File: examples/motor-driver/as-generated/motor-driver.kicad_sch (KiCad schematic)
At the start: 18 parts, among them J1 VM 2.7-10.8V, J2 MOTOR A, J3 MOTOR B, J4 LOGIC, U1 DRV8833PW

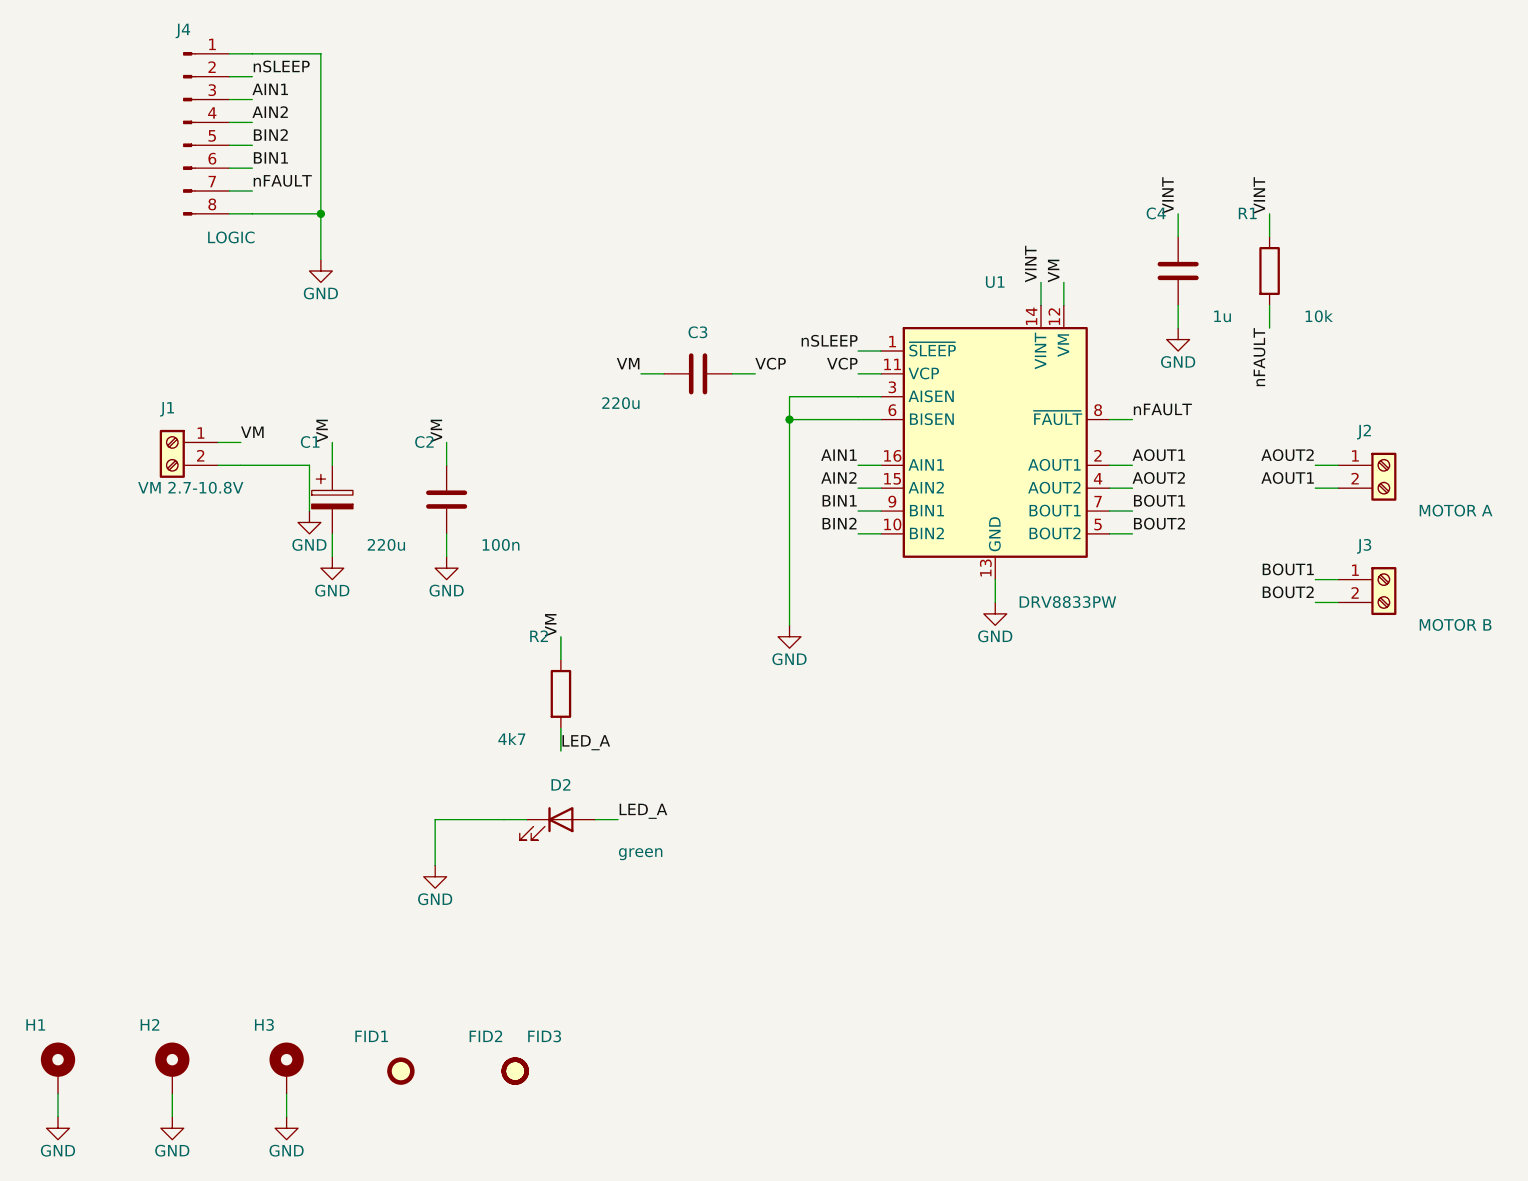
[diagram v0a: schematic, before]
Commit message: chore(examples): publish DRC-clean motor rebuild and verified copper renders
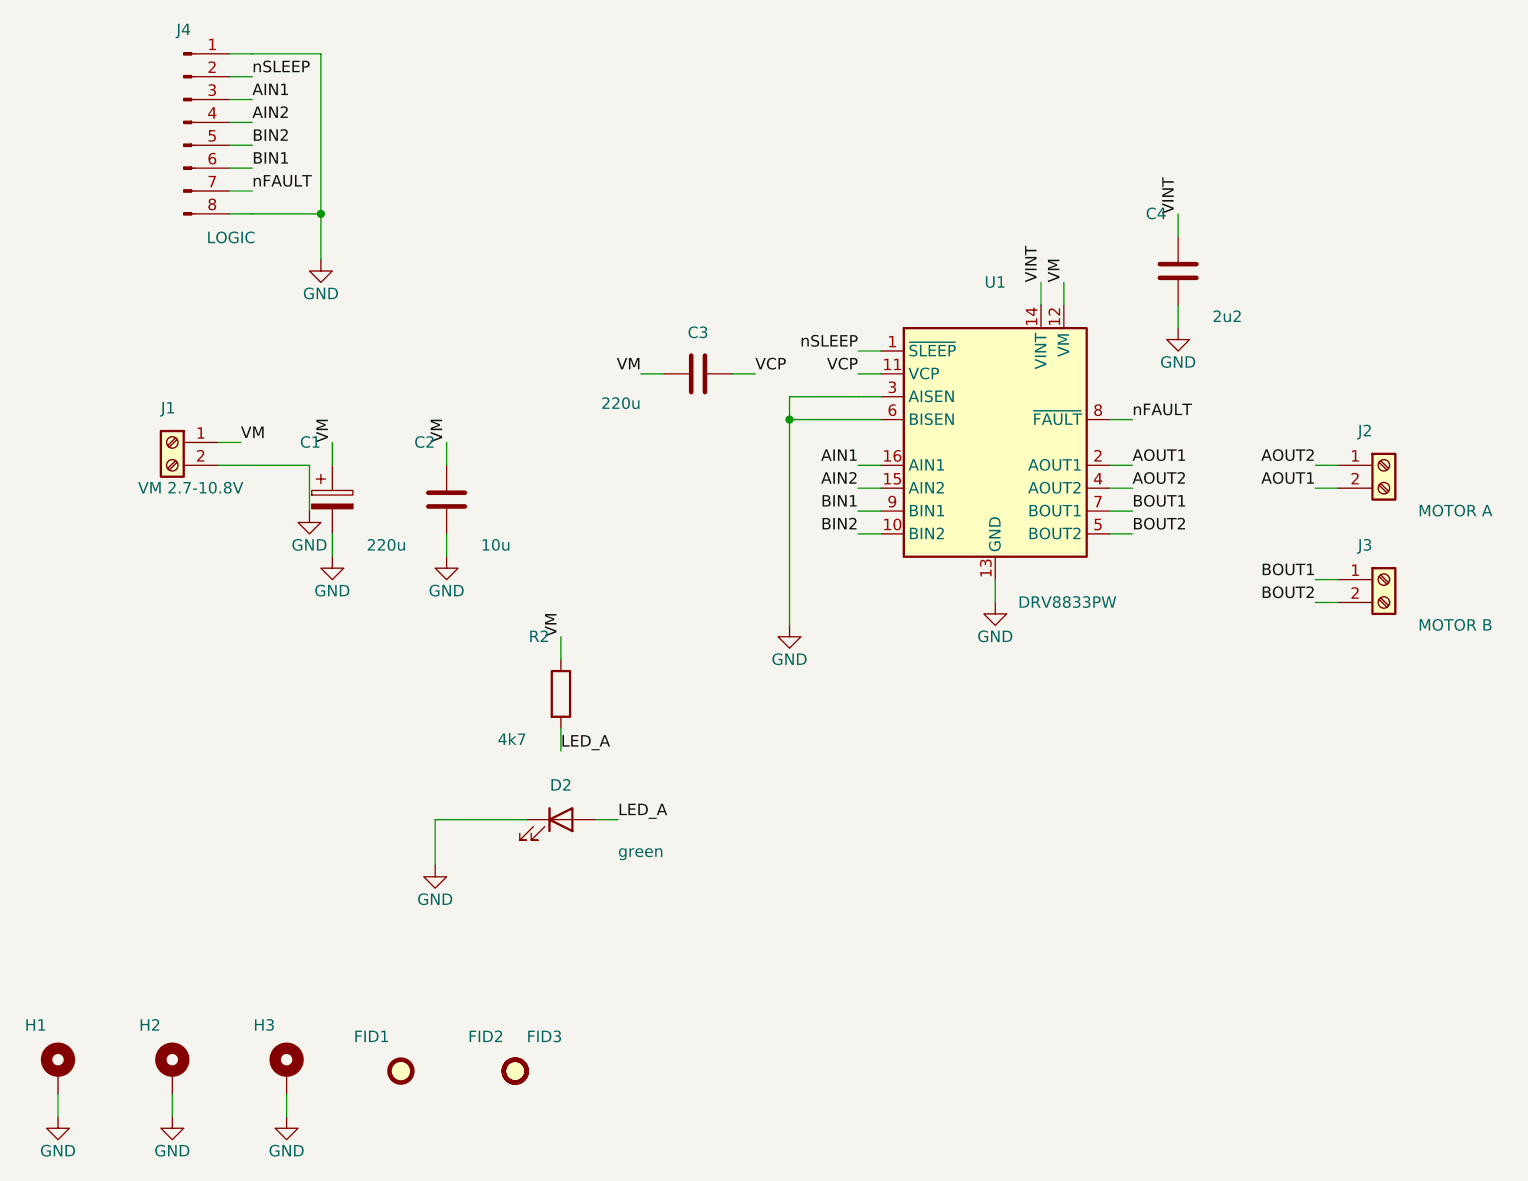
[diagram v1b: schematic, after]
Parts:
- removed R1: 10k, Resistor_SMD:R_0805_2012Metric, symbol Device:R
- C2: value 100n -> 10u
- C4: value 1u -> 2u2
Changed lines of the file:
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@@
     (exclude_from_sim no) (in_bom yes) (on_board yes) (dnp no)
     (property "Reference" "C2" (at 67.62 79.82 0) (effects (font (size 1.27 1.27)) (justify right)))
-    (property "Value" "100n" (at 72.7 91.25 0) (effects (font (size 1.27 1.27)) (justify left)))
+    (property "Value" "10u" (at 72.7 91.25 0) (effects (font (size 1.27 1.27)) (justify left)))
     (property "Footprint" "Capacitor_SMD:C_0805_2012Metric" (at 68.89 86.17 0) (effects (font (size 1.27 1.27)) hide))
-    (property "Datasheet" "https://product.samsungsem.com/mlcc/CL21B104KBCNNNC.do" (at 68.89 86.17 0) (effects (font (size 1.27 1.27)) hide))
+    (property "Datasheet" "https://weblib.samsungsem.com/mlcc/mlcc-ec-data-sheet.do?partNumber=CL21A106KAYNNN" (at 68.89 86.17 0) (effects (font (size 1.27 1.27)) hide))
     (pin "1" (uuid "b7b2b41f-3515-564d-8b3a-35316c1ea4a7-p1"))
     (pin "2" (uuid "b7b2b41f-3515-564d-8b3a-35316c1ea4a7-p2"))
@@
     (exclude_from_sim no) (in_bom yes) (on_board yes) (dnp no)
     (property "Reference" "C4" (at 148.9 54.42 0) (effects (font (size 1.27 1.27)) (justify right)))
-    (property "Value" "1u" (at 153.98 65.85 0) (effects (font (size 1.27 1.27)) (justify left)))
+    (property "Value" "2u2" (at 153.98 65.85 0) (effects (font (size 1.27 1.27)) (justify left)))
     (property "Footprint" "Capacitor_SMD:C_0805_2012Metric" (at 150.17 60.77 0) (effects (font (size 1.27 1.27)) hide))
-    (property "Datasheet" "https://product.samsungsem.com/mlcc/CL21A105KBFNNNE.do" (at 150.17 60.77 0) (effects (font (size 1.27 1.27)) hide))
+    (property "Datasheet" "https://weblib.samsungsem.com/mlcc/mlcc-ec-data-sheet.do?partNumber=CL21A225KAFNNN" (at 150.17 60.77 0) (effects (font (size 1.27 1.27)) hide))
     (pin "1" (uuid "016a090a-6346-5e98-b34f-0c93e38b6a13-p1"))
     (pin "2" (uuid "016a090a-6346-5e98-b34f-0c93e38b6a13-p2"))
     (instances (project "motor-driver" (path "/bddeec65-fa67-5f6a-9af2-d98e98d56e38" (reference "C4") (unit 1))))
   )
-  (wire (pts (xy 160.33 56.96) (xy 160.33 54.42)) (stroke (width 0) (type default)))
-  (label "VINT" (at 160.33 54.42 90) (effects (font (size 1.27 1.27)) (justify left bottom)))
-  (wire (pts (xy 160.33 64.58) (xy 160.33 67.12)) (stroke (width 0) (type default)))
-  (label "nFAULT" (at 160.33 67.12 90) (effects (font (size 1.27 1.27)) (justify right bottom)))
-  (symbol (lib_id "Device:R") (at 160.33 60.77 0.0) (unit 1)
-    (exclude_from_sim no) (in_bom yes) (on_board yes) (dnp no)
-    (property "Reference" "R1" (at 159.06 54.42 0) (effects (font (size 1.27 1.27)) (justify right)))
-    (property "Value" "10k" (at 164.14 65.85 0) (effects (font (size 1.27 1.27)) (justify left)))
-    (property "Footprint" "Resistor_SMD:R_0805_2012Metric" (at 160.33 60.77 0) (effects (font (size 1.27 1.27)) hide))
-    (property "Datasheet" "https://www.yageo.com/upload/media/product/productsearch/datasheet/rchip/PYu-RC_Group_51_RoHS_L_12.pdf" (at 160.33 60.77 0) (effects (font (size 1.27 1.27)) hide))
-    (pin "1" (uuid "366be20e-cb84-546e-97c6-cf2eae1f4272-p1"))
-    (pin "2" (uuid "366be20e-cb84-546e-97c6-cf2eae1f4272-p2"))
-    (instances (project "motor-driver" (path "/bddeec65-fa67-5f6a-9af2-d98e98d56e38" (reference "R1") (unit 1))))
-  )
   (wire (pts (xy 81.59 103.95) (xy 81.59 101.41)) (stroke (width 0) (type default)))
